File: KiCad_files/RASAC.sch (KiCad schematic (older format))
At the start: 0 parts

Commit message: Added VGA
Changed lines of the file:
@@
 S 6500 3800 1550 900
 U 5C14F3D5
-F0 "HDMI" 60
-F1 "HDMI.sch" 60
+F0 "HDMI_VGA" 60
+F1 "HDMI_VGA.sch" 60
 $EndSheet
 $EndSCHEMATC

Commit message: DDR RAM 32 bits instead of 64bits
Don't have enough pins :(
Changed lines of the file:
@@
 $Descr A4 11693 8268
 encoding utf-8
-Sheet 1 13
+Sheet 1 10
 Title "Reconfigurable Application-Specific Accelerator Card"
 Date "2018-11-27"
@@
 $EndSheet
 $Sheet
-S 8300 2450 1450 950
-U 5C14BDED
-F0 "DDR4_3" 60
-F1 "DDR4_3.sch" 60
-$EndSheet
-$Sheet
-S 3000 3800 1400 900
-U 5C14CE40
-F0 "DDR4_4" 60
-F1 "DDR4_4.sch" 60
-$EndSheet
-$Sheet
-S 4700 3800 1550 900
-U 5C14DE5B
-F0 "DDR4_things" 60
-F1 "DDR4_things.sch" 60
-$EndSheet
-$Sheet
-S 6500 3800 1550 900
+S 8300 2450 1550 900
 U 5C14F3D5
 F0 "HDMI_VGA" 60

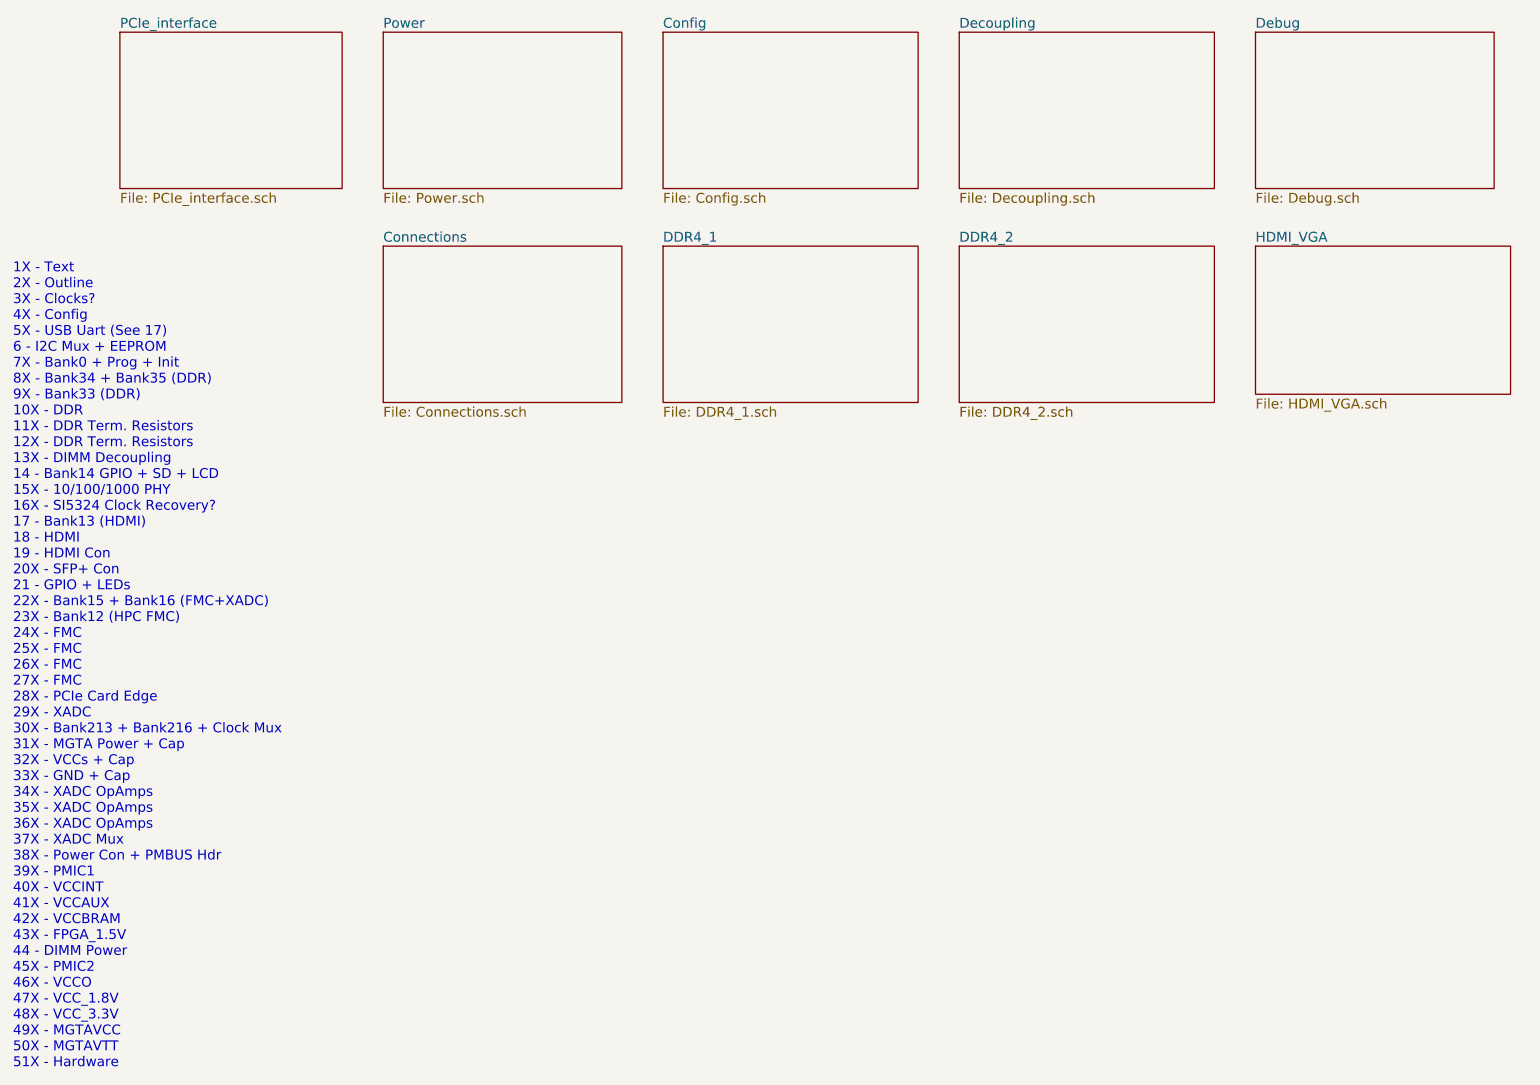
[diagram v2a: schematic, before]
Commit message: Cleanup for demo/presentation
Merged Config and Debug sheets.
Added GPIO for remaining pins.
Annotations.
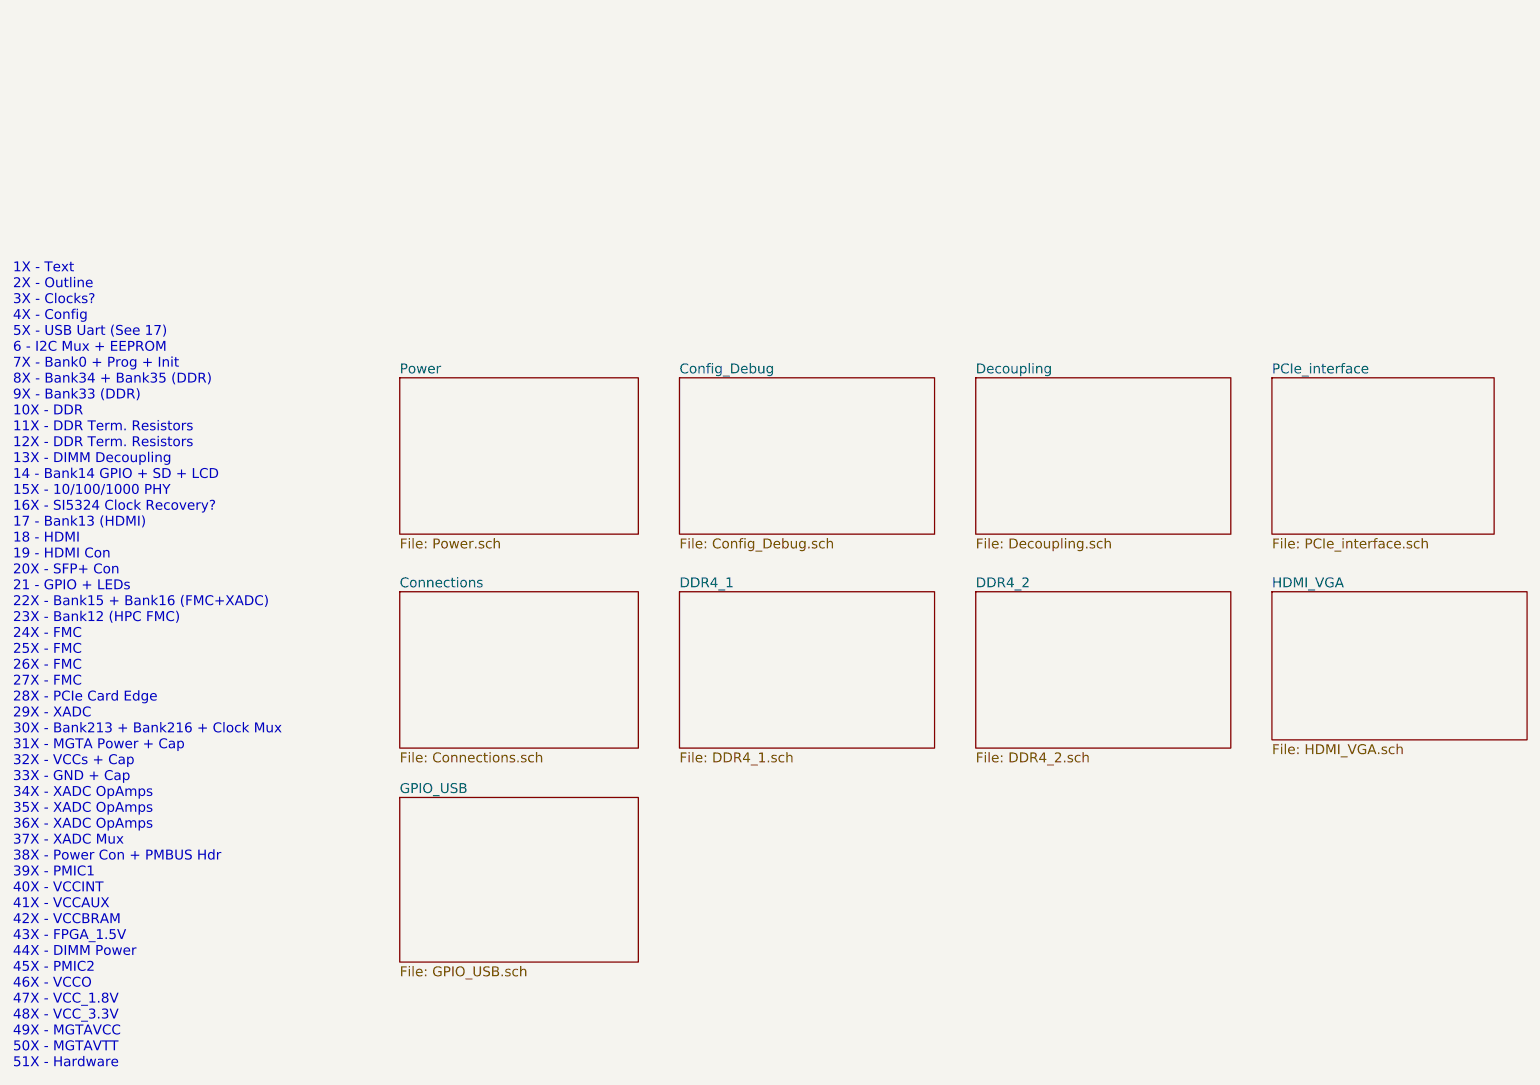
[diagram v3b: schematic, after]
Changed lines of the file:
@@
 $EndDescr
 $Sheet
-S 1400 1150 1350 950
+S 8400 3250 1350 950
 U 5BFDC338
 F0 "PCIe_interface" 60
@@
 $EndSheet
 $Sheet
-S 3000 1150 1450 950
+S 3100 3250 1450 950
 U 5BFDDAF0
 F0 "Power" 60
@@
 $EndSheet
 $Sheet
-S 4700 1150 1550 950
+S 4800 3250 1550 950
 U 5C0630AC
-F0 "Config" 60
-F1 "Config.sch" 60
+F0 "Config_Debug" 60
+F1 "Config_Debug.sch" 60
 $EndSheet
 $Sheet
-S 6500 1150 1550 950
+S 6600 3250 1550 950
 U 5C068931
 F0 "Decoupling" 60
@@
 $EndSheet
 Text Notes 750  7450 0    60   ~ 0
-1X - Text\n2X - Outline\n3X - Clocks?\n4X - Config\n5X - USB Uart (See 17)\n6 - I2C Mux + EEPROM\n7X - Bank0 + Prog + Init\n8X - Bank34 + Bank35 (DDR)\n9X - Bank33 (DDR)\n10X - DDR\n11X - DDR Term. Resistors\n12X - DDR Term. Resistors\n13X - DIMM Decoupling\n14 - Bank14 GPIO + SD + LCD\n15X - 10/100/1000 PHY\n16X - SI5324 Clock Recovery?\n17 - Bank13 (HDMI)\n18 - HDMI\n19 - HDMI Con\n20X - SFP+ Con\n21 - GPIO + LEDs\n22X - Bank15 + Bank16 (FMC+XADC)\n23X - Bank12 (HPC FMC)\n24X - FMC\n25X - FMC\n26X - FMC\n27X - FMC\n28X - PCIe Card Edge\n29X - XADC\n30X - Bank213 + Bank216 + Clock Mux\n31X - MGTA Power + Cap\n32X - VCCs + Cap\n33X - GND + Cap\n34X - XADC OpAmps\n35X - XADC OpAmps\n36X - XADC OpAmps\n37X - XADC Mux\n38X - Power Con + PMBUS Hdr\n39X - PMIC1\n40X - VCCINT\n41X - VCCAUX\n42X - VCCBRAM\n43X - FPGA_1.5V\n44 - DIMM Power\n45X - PMIC2\n46X - VCCO\n47X - VCC_1.8V\n48X - VCC_3.3V\n49X - MGTAVCC\n50X - MGTAVTT\n51X - Hardware
+1X - Text\n2X - Outline\n3X - Clocks?\n4X - Config\n5X - USB Uart (See 17)\n6 - I2C Mux + EEPROM\n7X - Bank0 + Prog + Init\n8X - Bank34 + Bank35 (DDR)\n9X - Bank33 (DDR)\n10X - DDR\n11X - DDR Term. Resistors\n12X - DDR Term. Resistors\n13X - DIMM Decoupling\n14 - Bank14 GPIO + SD + LCD\n15X - 10/100/1000 PHY\n16X - SI5324 Clock Recovery?\n17 - Bank13 (HDMI)\n18 - HDMI\n19 - HDMI Con\n20X - SFP+ Con\n21 - GPIO + LEDs\n22X - Bank15 + Bank16 (FMC+XADC)\n23X - Bank12 (HPC FMC)\n24X - FMC\n25X - FMC\n26X - FMC\n27X - FMC\n28X - PCIe Card Edge\n29X - XADC\n30X - Bank213 + Bank216 + Clock Mux\n31X - MGTA Power + Cap\n32X - VCCs + Cap\n33X - GND + Cap\n34X - XADC OpAmps\n35X - XADC OpAmps\n36X - XADC OpAmps\n37X - XADC Mux\n38X - Power Con + PMBUS Hdr\n39X - PMIC1\n40X - VCCINT\n41X - VCCAUX\n42X - VCCBRAM\n43X - FPGA_1.5V\n44X - DIMM Power\n45X - PMIC2\n46X - VCCO\n47X - VCC_1.8V\n48X - VCC_3.3V\n49X - MGTAVCC\n50X - MGTAVTT\n51X - Hardware
 $Sheet
-S 8300 1150 1450 950
-U 5C069176
-F0 "Debug" 60
-F1 "Debug.sch" 60
-$EndSheet
-$Sheet
-S 3000 2450 1450 950
+S 3100 4550 1450 950
 U 5C064F83
 F0 "Connections" 60
@@
 $EndSheet
 $Sheet
-S 4700 2450 1550 950
+S 4800 4550 1550 950
 U 5C0652F6
 F0 "DDR4_1" 60
@@
 $EndSheet
 $Sheet
-S 6500 2450 1550 950
+S 6600 4550 1550 950
 U 5C14AAFF
 F0 "DDR4_2" 60
@@
 $EndSheet
 $Sheet
-S 8300 2450 1550 900
+S 8400 4550 1550 900
 U 5C14F3D5
 F0 "HDMI_VGA" 60
 F1 "HDMI_VGA.sch" 60
 $EndSheet
+$Sheet
+S 3100 5800 1450 1000
+U 5C199E81
+F0 "GPIO_USB" 60
+F1 "GPIO_USB.sch" 60
+$EndSheet
 $EndSCHEMATC

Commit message: Cleanup + Update to KiCad 5.0 + DDR2
Updated to KiCad 5, which re-organized libraries, so corrected them to not need RASAC-rescue.lib.
Also cleaned up some stuff.
DDR4 has been removed and in place will be DDR2.
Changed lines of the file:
@@
-EESchema Schematic File Version 2
-LIBS:power
-LIBS:device
-LIBS:switches
-LIBS:relays
-LIBS:motors
-LIBS:transistors
-LIBS:conn
-LIBS:linear
-LIBS:regul
-LIBS:74xx
-LIBS:cmos4000
-LIBS:adc-dac
-LIBS:memory
-LIBS:xilinx
-LIBS:microcontrollers
-LIBS:dsp
-LIBS:microchip
-LIBS:analog_switches
-LIBS:motorola
-LIBS:texas
-LIBS:intel
-LIBS:audio
-LIBS:interface
-LIBS:digital-audio
-LIBS:philips
-LIBS:display
-LIBS:cypress
-LIBS:siliconi
-LIBS:opto
-LIBS:atmel
-LIBS:contrib
-LIBS:valves
-LIBS:custom
-LIBS:Connector
+EESchema Schematic File Version 4
 LIBS:RASAC-cache
-EELAYER 25 0
+EELAYER 26 0
 EELAYER END
 $Descr A4 11693 8268
@@
 S 4800 4550 1550 950
 U 5C0652F6
-F0 "DDR4_1" 60
-F1 "DDR4_1.sch" 60
+F0 "DDR2_1" 60
+F1 "DDR2_1.sch" 60
 $EndSheet
 $Sheet
 S 6600 4550 1550 950
 U 5C14AAFF
-F0 "DDR4_2" 60
-F1 "DDR4_2.sch" 60
+F0 "DDR2_2" 60
+F1 "DDR2_2.sch" 60
 $EndSheet
 $Sheet

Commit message: HDMI_VGA is good. Need 5V for HDMI
TODO: DDR2, connections, power
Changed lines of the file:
@@
 $Descr A4 11693 8268
 encoding utf-8
-Sheet 1 10
+Sheet 1 9
 Title "Reconfigurable Application-Specific Accelerator Card"
 Date "2018-11-27"
@@
 F1 "HDMI_VGA.sch" 60
 $EndSheet
-$Sheet
-S 3100 5800 1450 1000
-U 5C199E81
-F0 "GPIO_USB" 60
-F1 "GPIO_USB.sch" 60
-$EndSheet
 $EndSCHEMATC
